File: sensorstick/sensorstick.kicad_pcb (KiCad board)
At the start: 4 copper layers, 39.2 x 28.4 mm, 24 parts, among them J1 USB-A Header, U1 ESP32-C3_SUPERMINI, U2 SGP30, U3 SHT4x, U4 SCD40-D-R2, U5 PCA9306DC, U6 LP5907MFX-1.8

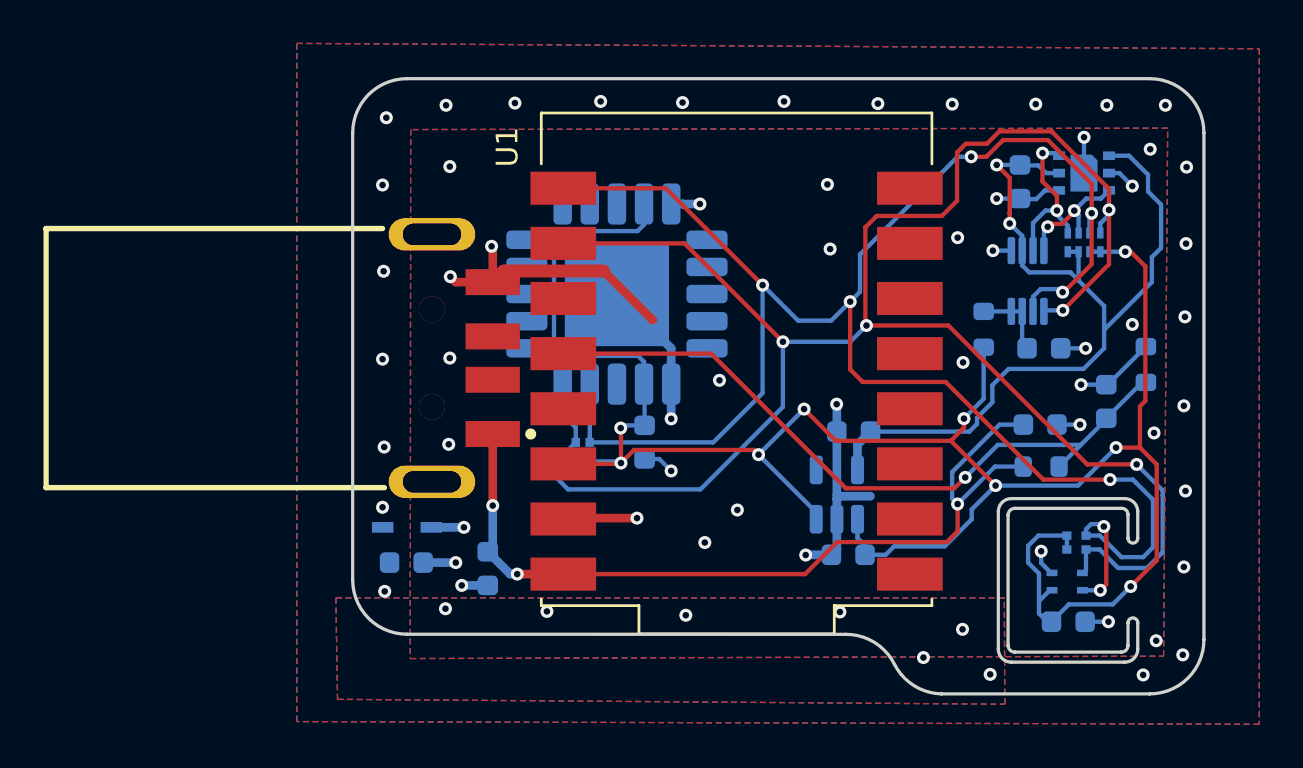
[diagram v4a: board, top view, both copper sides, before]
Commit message: changed sgp30 to sgp
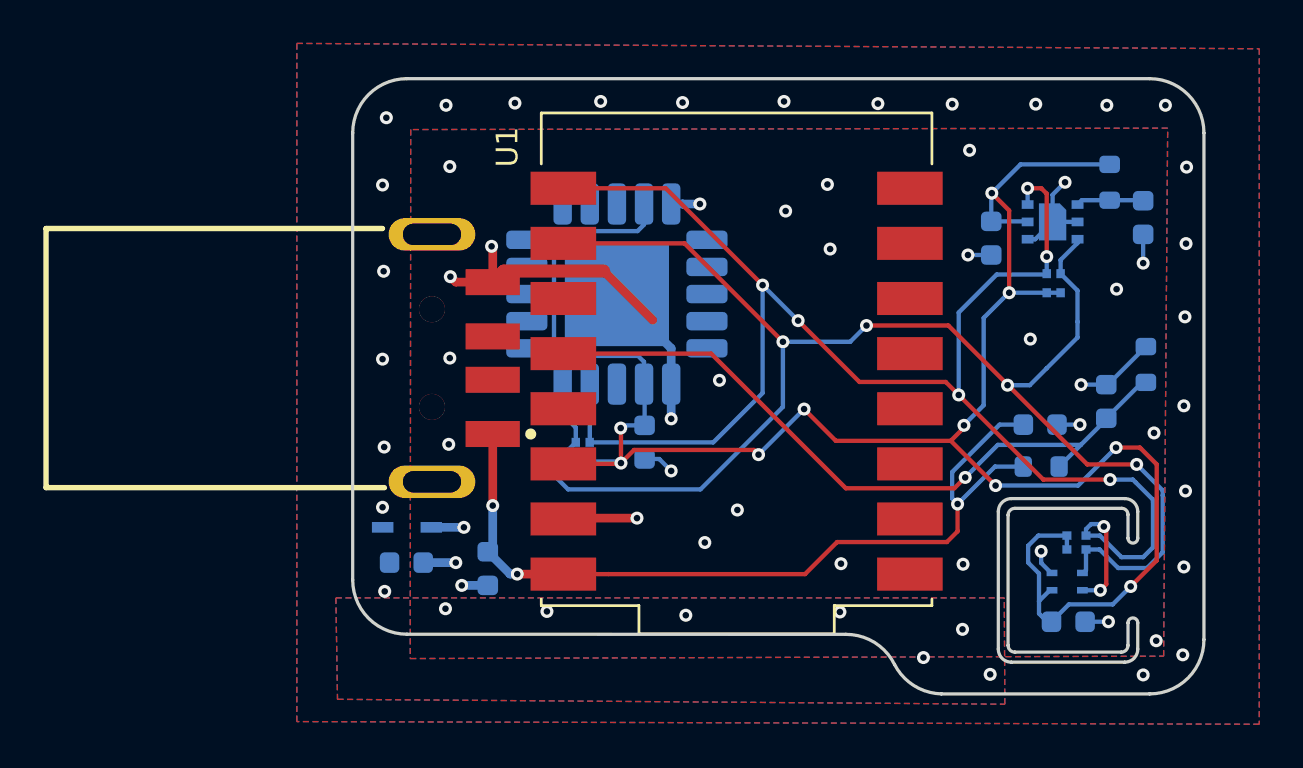
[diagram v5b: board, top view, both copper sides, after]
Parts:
- removed C7, C8: 1µF, Capacitor_SMD:C_0603_1608Metric
- removed U2: SGP30, SGP30:SGP30
- removed U5: PCA9306DC, Package_SO:VSSOP-8_2.3x2mm_P0.5mm
- removed U6: LP5907MFX-1.8, Package_TO_SOT_SMD:SOT-23-5
- added U7: SGP41, SGP41_D_R4:XDCR_SGP41-D-R4, B.Cu at (91.5, 92.2)
- C2, C6: value 100nF -> 1μF
- R1: value 200 kΩ -> 4.7 Ω
- R2: value 10 kΩ -> 33kΩ
- RN1, RN2: value 2x 100k Array -> 2x 10k Array
- RN3: value 4x 100k Array -> 2x 10k Array; footprint easyeda2kicad:RES-ARRAY-SMD_0402-8P-L2.0-W1.0-BL -> easyeda2kicad:RES-ARRAY-SMD_0402-4P-L1.0-W1.0-BL
- TH1: value 10 kΩ NTC -> 33kΩ NTC
- U4: value SCD40-D-R2 -> SCD40
- moved R1 8.92 mm to (94.2, 90.4)
- moved C6 7.57 mm to (95.7, 92.0), turned to -90 degrees
- moved C2 2.92 mm to (88.7, 93.0), turned to 90 degrees
- moved RN3 2.34 mm to (91.6, 95.0), turned to -90 degrees
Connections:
- C2 pad 1: +1.8V -> GND
- C2 pad 2: GND -> +3.3V
- C6 pad 1: Net-(U5-EN) -> Net-(U7-VDD)
- R1 pad 1: +3.3V -> Net-(U7-VDD)
- R1 pad 2: Net-(U5-EN) -> +3.3V
- RN3 pad 3: /IC2_SDA_1.8 -> +3.3V
- RN3 pad 4: /I2C_SCL_1.8 -> +3.3V
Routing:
- net +1.8V: track 42.1 -> 0.00 mm, vias 2 -> 0
- net /IC2_SDA_3.3: track 90.0 -> 70.7 mm, vias 5 -> 4
- net /I2C_SCL_3.3: track 88.1 -> 74.9 mm
- net GND: track 54.5 -> 43.8 mm, vias 34 -> 32
- net /I2C_SCL_1.8: track 7.59 -> 0.00 mm, vias 2 -> 0
- net /IC2_SDA_1.8: track 5.88 -> 0.00 mm, vias 2 -> 0
- net +3.3V: track 102.3 -> 96.8 mm, vias 9 -> 10
- net Net-(U5-EN): track 3.57 -> 0.00 mm
- net Net-(U7-VDD): track 0.00 -> 3.44 mm

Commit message: added VEML7700
because of moving from SGP30 to SGP41 I got rid of everything handling 1.8V and 1.8V I²C with space on the pcb I now filled with a High Accuracy Ambient Light Sensor
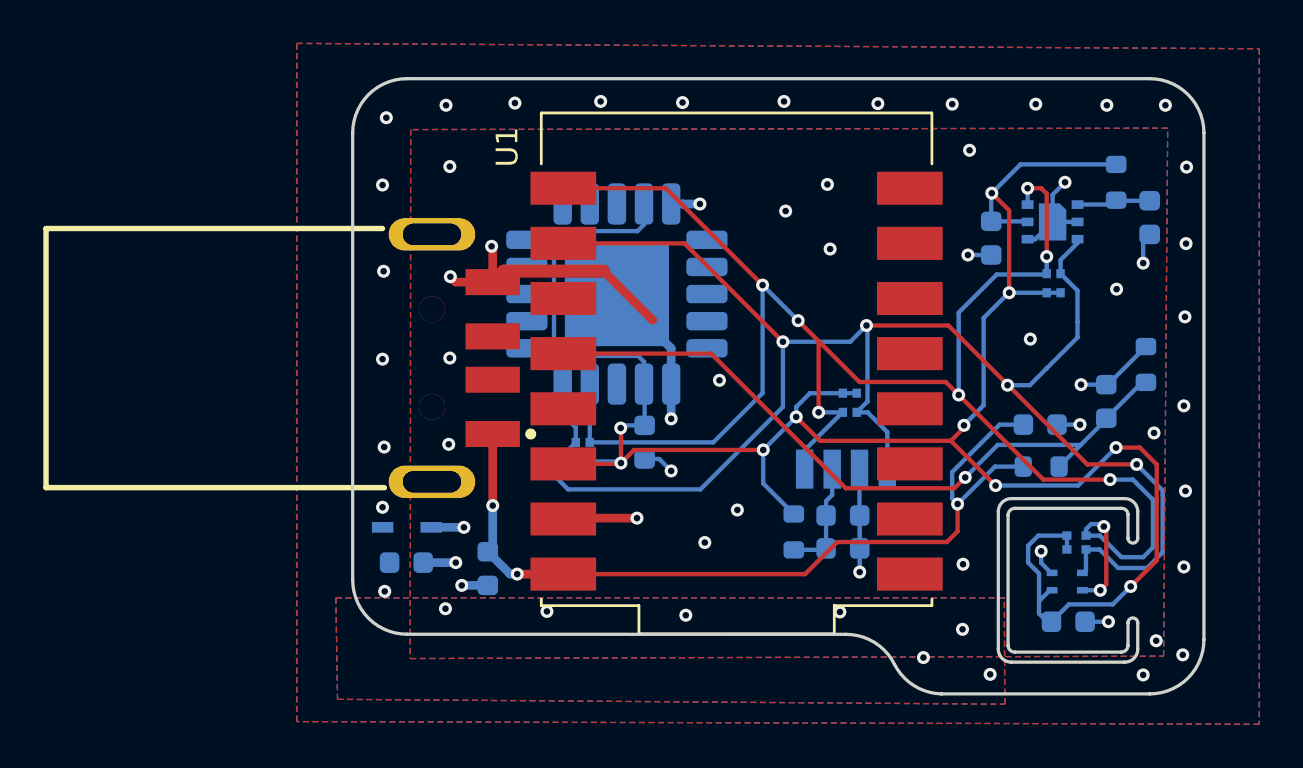
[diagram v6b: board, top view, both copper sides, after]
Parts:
- added C7: 100nF, Capacitor_SMD:C_0603_1608Metric, B.Cu at (81.9, 105.8)
- added C8: 10μF, Capacitor_SMD:C_0603_1608Metric, B.Cu at (81.9, 107.3)
- added LED1: VEML7700, easyeda2kicad:LED-SMD_4P-L6.8-W2.4_VEML7700-TR, B.Cu at (82.0, 103.6)
- added R3: 10Ω, Resistor_SMD:R_0603_1608Metric, B.Cu at (79.6, 106.5)
- added RN4: 2x 10k Array, easyeda2kicad:RES-ARRAY-SMD_0402-4P-L1.0-W1.0-BL, B.Cu at (82.2, 100.6)
- U3: value SHT4x -> WSEN-HIDS
- moved C6 0.30 mm to (96.0, 92.0)
- moved R1 0.30 mm to (94.5, 90.4)
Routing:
- net /I2C_SCL_3.3: track 74.9 -> 82.6 mm, vias 8 -> 9
- net /IC2_SDA_3.3: track 70.7 -> 78.5 mm
- net +3.3V: track 96.8 -> 103.7 mm
- net Net-(LED1-VDD): track 0.00 -> 5.28 mm
- net GND: track 43.8 -> 48.6 mm
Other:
- board text added: "${TITLE} by ${COMPANY} (rev. 2.1) ${COMMENT1}"
- board text removed: "${TITLE} by ${COMPANY} (rev. 2) ${COMMENT1}"
